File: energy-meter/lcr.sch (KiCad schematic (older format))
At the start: 46 parts, among them Q10 AP3400, Q11 AP3400, Q12 AP3400, Q14 AP3400, U10 SLG47004, U11 SLG47004, U12 SLG47004, U13 XC6227C381MR-G

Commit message: continue changing schematic
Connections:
- wire segments 177 -> 183
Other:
- note added: "6V AC -> 8.5V p-p\n"
- note added: "FIXME:\n- connect input of OpAmps to analog switch to calibrate offset?\n (probably not required for AC)\n- don't use Kelvin measurement for resistors\n -> frees up some analog switches\n- get rid of U10, which is hardly used anymore\n- OUT1=CURR0\n- OUT0B=CURR1\n- VDDA can be 3.3V, I think\n- bias one side of OpAmp to VCC/2"
- note removed: "FIXME:\n- connect input of OpAmps to analog switch to calibrate offset?\n (probably not required for AC)\n- don't use Kelvin measurement for resistors\n -> frees up some analog switches\n- get rid of U10, which is hardly used anymore\n- OUT1=CURR0\n- OUT0B=CURR1\n- VDDA can be 3.3V, I think"
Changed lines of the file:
@@
 CURR1
 Text Notes 12250 4400 0    50   ~ 0
-FIXME:\n- connect input of OpAmps to analog switch to calibrate offset?\n  (probably not required for AC)\n- don't use Kelvin measurement for resistors\n  -> frees up some analog switches\n- get rid of U10, which is hardly used anymore\n- OUT1=CURR0\n- OUT0B=CURR1\n- VDDA can be 3.3V, I think
+FIXME:\n- connect input of OpAmps to analog switch to calibrate offset?\n  (probably not required for AC)\n- don't use Kelvin measurement for resistors\n  -> frees up some analog switches\n- get rid of U10, which is hardly used anymore\n- OUT1=CURR0\n- OUT0B=CURR1\n- VDDA can be 3.3V, I think\n- bias one side of OpAmp to VCC/2
+Wire Wire Line
+	10800 2750 10800 2650
+Wire Wire Line
+	10800 2650 10650 2650
+Connection ~ 10800 2750
+Wire Wire Line
+	10550 3100 10550 3000
+Wire Wire Line
+	10550 3000 10400 3000
+Connection ~ 10400 3000
+Wire Wire Line
+	9750 3550 9750 3300
+Wire Wire Line
+	9750 3300 9900 3300
+Connection ~ 9900 3300
+Text Notes 11850 5800 0    50   ~ 0
+6V AC -> 8.5V p-p\n
 $EndSCHEMATC

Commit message: remove two of the opamps
We can measure the voltage without an amplifier so let's do it. The other
was used for the LCR outputs, which we don't have here.
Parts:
- removed C65, C67, C70, C72: 100n, Capacitor_SMD:C_0603_1608Metric_Pad1.05x0.95mm_HandSolder, symbol Device:C
- removed C79, C80: 4.7p, Capacitor_SMD:C_0603_1608Metric_Pad1.05x0.95mm_HandSolder, symbol Device:C
- removed C81, C82: 1u, Capacitor_SMD:C_0805_2012Metric_Pad1.15x1.40mm_HandSolder, symbol Device:C
- removed FB1, FB3: 600R, 0.5A, Inductor_SMD:L_0603_1608Metric_Pad1.05x0.95mm_HandSolder, symbol Device:Ferrite_Bead_Small
- removed JP20: SolderJumper_2_Open, Jumper:SolderJumper-2_P1.3mm_Open_RoundedPad1.0x1.5mm, symbol Jumper:SolderJumper_2_Open
- removed Q12, Q14: AP3400, Package_TO_SOT_SMD:SOT-23_Handsoldering, symbol Device:Q_NMOS_GSD
- removed R67, R68, R69: 1k, Resistor_SMD:R_0603_1608Metric_Pad1.05x0.95mm_HandSolder, symbol Device:R
- removed R70, R71: 10k, Resistor_SMD:R_0603_1608Metric_Pad1.05x0.95mm_HandSolder, symbol Device:R
- removed R79, R80: 47k, Resistor_SMD:R_0603_1608Metric_Pad1.05x0.95mm_HandSolder, symbol Device:R
- removed R84: 20R, 100 mW, 0.1%, glowstone:R_0603_1608Metric_Pad1.05x0.95mm_HandSolder_Shunt, symbol Device:R_Shunt
- removed R86: 2M, 0.1%, glowstone:R_1210_3225Metric_Pad1.42x2.65mm_HandSolder_Shunt, symbol Device:R_Shunt
- removed R95: 1R, 0.1% (alternative to 2M), glowstone:R_1210_3225Metric_Pad1.42x2.65mm_HandSolder_Shunt, symbol Device:R_Shunt
- removed U10, U12: SLG47004, glowstone:SLG47004, symbol glowstone:SLG47004
- removed U13: XC6227C381MR-G, Package_TO_SOT_SMD:SOT-23-5_HandSoldering, symbol Regulator_Linear:TLV75509PDBV
- added C84: 270p, 1%, Capacitor_SMD:C_0603_1608Metric_Pad1.05x0.95mm_HandSolder, symbol Device:C
- added L4: 470u, Inductor_SMD:L_1210_3225Metric_Pad1.42x2.65mm_HandSolder, symbol Device:L
- added R90, R91: 1k, 1%, Resistor_SMD:R_0603_1608Metric_Pad1.05x0.95mm_HandSolder, symbol Device:R
- R64: value 20R, 100 mW, 0.1% -> 50k, 0.1%
- R85: value 10k, 0.1% -> 50R, 0.1%; footprint glowstone:R_0603_1608Metric_Pad1.05x0.95mm_HandSolder_Shunt -> Resistor_SMD:R_0603_1608Metric_Pad1.05x0.95mm_HandSolder; symbol Device:R_Shunt -> Device:R
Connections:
- net labels removed: 5V, AS0A_1, AS0A_3, AS1A_1, AS1A_3, DAC0, DAC1, OP2_OUT, OP2_OUT_F, OUT0, OUT01_SHORT, OUT0B, OUT1, TEMP2, VDDA1, VDDA3
- wire segments 183 -> 96
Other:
- note added: "FIXME:\n- connect inputs of OpAmp to MCU so it can short them for calibration\n- use resistor dividers to generate reference voltages for calibration,\n VCC side connected to MCU to turn them off\n\n- normal gain should be 4\n- gain 4000 and 4M would be good to have\n\n- add some LEDs for GD32V\n\n- relay\n\n- add optional DC/DC for 3V3 from T2"
- note added: "https://rf-tools.com/lc-filter/"
- note removed: "6V AC -> 8.5V p-p\n"
- note removed: "FIXME:\n- connect input of OpAmps to analog switch to calibrate offset?\n (probably not required for AC)\n- don't use Kelvin measurement for resistors\n -> frees up some analog switches\n- get rid of U10, which is hardly used anymore\n- OUT1=CURR0\n- OUT0B=CURR1\n- VDDA can be 3.3V, I think\n- bias one side of OpAmp to VCC/2"

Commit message: everything done except current measurement
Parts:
- removed D12: SP3012-06UTG, glowstone:UDFN-14_3.5x1.35mm_P0.5mm, symbol glowstone:SP3012-06UTG
- removed Q10: AP3400, Package_TO_SOT_SMD:SOT-23, symbol Device:Q_NMOS_GSD
- removed R54, R55: 10k, Resistor_SMD:R_0603_1608Metric_Pad1.05x0.95mm_HandSolder, symbol Device:R
- Q11: footprint Package_TO_SOT_SMD:SOT-23 -> Package_TO_SOT_SMD:SOT-23_Handsoldering
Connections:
- net labels removed: IN0, IN1, SCL_5V, SDA_5V, VOLTAGE0, VOLTAGE1
- wire segments 96 -> 61
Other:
- note added: "FIXME:\n- connect inputs of OpAmp to MCU so it can short them for calibration\n- use resistor dividers to generate reference voltages for calibration,\n VCC side connected to MCU to turn them off\n\n- normal gain should be 4\n- gain 4000 and 4M would be good to have\n\n- add some LEDs for GD32V\n\n- relay\n\n- add optional DC/DC for 3V3 from T2\n\n- remove LC filter and replace by one that is bef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"
- note removed: "FIXME:\n- connect inputs of OpAmp to MCU so it can short them for calibration\n- use resistor dividers to generate reference voltages for calibration,\n VCC side connected to MCU to turn them off\n\n- normal gain should be 4\n- gain 4000 and 4M would be good to have\n\n- add some LEDs for GD32V\n\n- relay\n\n- add optional DC/DC for 3V3 from T2"
- moved on the sheet: R52, R53

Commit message: DRC, add header for I2C
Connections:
- net labels removed: VDDA
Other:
- note added: "FIXME:\n- connect inputs of OpAmp to MCU so it can short them for calibration\n- use resistor dividers to generate reference voltages for calibration,\n VCC side connected to MCU to turn them off\n\n- normal gain should be 4\n- gain 4000 and 4M would be good to have\n\n- remove LC filter and replace by one that is before the opamp?"
- note removed: "FIXME:\n- connect inputs of OpAmp to MCU so it can short them for calibration\n- use resistor dividers to generate reference voltages for calibration,\n VCC side connected to MCU to turn them off\n\n- normal gain should be 4\n- gain 4000 and 4M would be good to have\n\n- add some LEDs for GD32V\n\n- relay\n\n- add optional DC/DC for 3V3 from T2\n\n- remove LC filter and replace by one that is bef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"
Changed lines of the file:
@@
-$EndComp
-$Comp
-L power:VDDA #PWR0119
-U 1 1 605C4057
-P 3900 5650
-F 0 "#PWR0119" H 3900 5500 50  0001 C CNN
-F 1 "VDDA" H 3917 5823 50  0000 C CNN
-F 2 "" H 3900 5650 50  0001 C CNN
-F 3 "" H 3900 5650 50  0001 C CNN
-	1    3900 5650
-	1    0    0    -1
 $EndComp
 $Comp
@@
 CURR1
 Text Notes 12250 4400 0    50   ~ 0
-FIXME:\n- connect inputs of OpAmp to MCU so it can short them for calibration\n- use resistor dividers to generate reference voltages for calibration,\n  VCC side connected to MCU to turn them off\n\n- normal gain should be 4\n- gain 4000 and 4M would be good to have\n\n- add some LEDs for GD32V\n\n- relay\n\n- add optional DC/DC for 3V3 from T2\n\n- remove LC filter and replace by one that is before the opamp?
+FIXME:\n- connect inputs of OpAmp to MCU so it can short them for calibration\n- use resistor dividers to generate reference voltages for calibration,\n  VCC side connected to MCU to turn them off\n\n- normal gain should be 4\n- gain 4000 and 4M would be good to have\n\n- remove LC filter and replace by one that is before the opamp?
 Text Label 4600 4850 2    50   ~ 0
 CURR1
@@
 	0    1    1    0
 $EndComp
+$Comp
+L power:+3V3 #PWR0119
+U 1 1 60CCAFAF
+P 3900 5650
+F 0 "#PWR0119" H 3900 5500 50  0001 C CNN
+F 1 "+3V3" H 3915 5823 50  0000 C CNN
+F 2 "" H 3900 5650 50  0001 C CNN
+F 3 "" H 3900 5650 50  0001 C CNN
+	1    3900 5650
+	1    0    0    -1
+$EndComp
 $EndSCHEMATC

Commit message: 2nd relay needs an additional driver if we want to use both of them
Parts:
- removed Q11: AP3400, Package_TO_SOT_SMD:SOT-23_Handsoldering, symbol Device:Q_NMOS_GSD
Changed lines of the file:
@@
 Wire Wire Line
 	10100 2600 10100 3350
-$Comp
-L Device:Q_NMOS_GSD Q?
-U 1 1 6091EE3A
-P 12650 2100
-AR Path="/60846F2E/6091EE3A" Ref="Q?"  Part="1"
-AR Path="/60514CC5/6091EE3A" Ref="Q11"  Part="1"
-AR Path="/607B74C2/6091EE3A" Ref="Q11"  Part="1"
-F 0 "Q11" H 12856 2146 50  0000 L CNN
-F 1 "AP3400" H 12856 2055 50  0000 L CNN
-F 2 "Package_TO_SOT_SMD:SOT-23_Handsoldering" H 12850 2200 50  0001 C CNN
-F 3 "https://datasheet.lcsc.com/szlcsc/1901071504_ShenZhen-Quan-Li-Semiconductor-AP3400_C353070.pdf" H 12650 2100 50  0001 C CNN
-F 4 "AP3400, C353070, HSS2306A, C518790, AO3400A, C700953" H 12650 2100 50  0001 C CNN "LCSC"
-	1    12650 2100
-	0    1    1    0
-$EndComp
 Text HLabel 2500 4850 0    50   Input ~ 0
 SDA

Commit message: adjust voltage divider to somewhat work if transformer is also used for VCC
In that case, we will only see one half of the wave.
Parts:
- added U2: MCP6V96T-E/OT, Package_TO_SOT_SMD:SOT-23-5, symbol Amplifier_Operational:MCP6L91T-EOT
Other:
- note added: "FIXME:\n- use OP07 as suggested here?\n https://datasheet.lcsc.com/szlcsc/1810010312_Qingxian-Zeming-Langxi-Elec-ZMCT104C_C84212.pdf\n -> first stage with MCP and similar to that ^^ (see my LTSpice simulation),\n second and third stage with 1000x gain, connect all intermediate signals to\n ADC so GD32 can choose gain by choosing the right signal\n- connect inputs of OpAmp to MCU so it can short t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"
- note removed: "FIXME:\n- connect inputs of OpAmp to MCU so it can short them for calibration\n- use resistor dividers to generate reference voltages for calibration,\n VCC side connected to MCU to turn them off\n\n- normal gain should be 4\n- gain 4000 and 4M would be good to have\n\n- remove LC filter and replace by one that is before the opamp?"
- note removed: "For 3.3V/2+-0.5V:\n49.45k and 65.55k"
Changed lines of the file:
@@
 Text Label 7500 2950 1    50   ~ 0
 VDDA2
-Text Notes 7600 4050 0    50   ~ 0
-For 3.3V/2+-0.5V:\n49.45k and 65.55k
 $Comp
 L Device:R R85
@@
 Text Label 8600 3350 0    50   ~ 0
 CURR1
-Text Notes 12250 4400 0    50   ~ 0
-FIXME:\n- connect inputs of OpAmp to MCU so it can short them for calibration\n- use resistor dividers to generate reference voltages for calibration,\n  VCC side connected to MCU to turn them off\n\n- normal gain should be 4\n- gain 4000 and 4M would be good to have\n\n- remove LC filter and replace by one that is before the opamp?
+Text Notes 7450 6100 0    50   ~ 0
+FIXME:\n- use OP07 as suggested here?\n  https://datasheet.lcsc.com/szlcsc/1810010312_Qingxian-Zeming-Langxi-Elec-ZMCT104C_C84212.pdf\n  -> first stage with MCP and similar to that ^^ (see my LTSpice simulation),\n  second and third stage with 1000x gain, connect all intermediate signals to\n  ADC so GD32 can choose gain by choosing the right signal\n- connect inputs of OpAmp to MCU so it can short them for calibration\n- use resistor dividers to generate reference voltages for calibration,\n  VCC side connected to MCU to turn them off\n\n- normal gain should be 4\n- gain 4000 and 4M would be good to have\n\n- remove LC filter and replace by one that is before the opamp?
 Text Label 4600 4850 2    50   ~ 0
 CURR1
@@
 	1    0    0    -1
 $EndComp
+$Comp
+L Amplifier_Operational:MCP6L91T-EOT U2
+U 1 1 60E518DB
+P 8750 2000
+F 0 "U2" H 9094 2046 50  0000 L CNN
+F 1 "MCP6V96T-E/OT" H 9094 1955 50  0000 L CNN
+F 2 "Package_TO_SOT_SMD:SOT-23-5" H 8650 1800 50  0001 L CNN
+F 3 "https://www.mouser.de/datasheet/2/268/MCP6V96_Family_Data_Sheet_DS20006467A-1948680.pdf" H 8750 2200 50  0001 C CNN
+	1    8750 2000
+	1    0    0    -1
+$EndComp

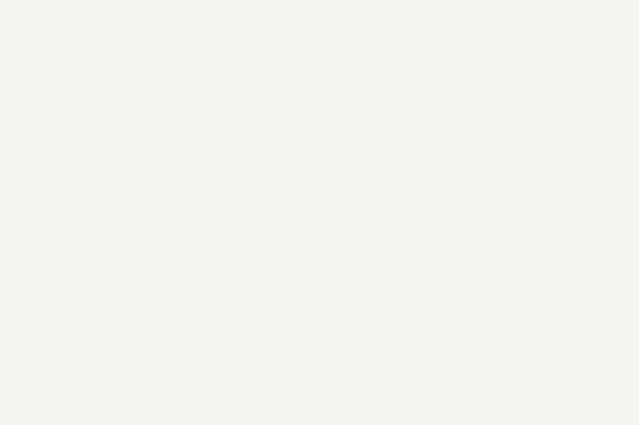
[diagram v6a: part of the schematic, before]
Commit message: use solid state relays for calibration
That way, we have enough space for two of them. The alternative relay
shares space with the other relay because only one of them will be used.
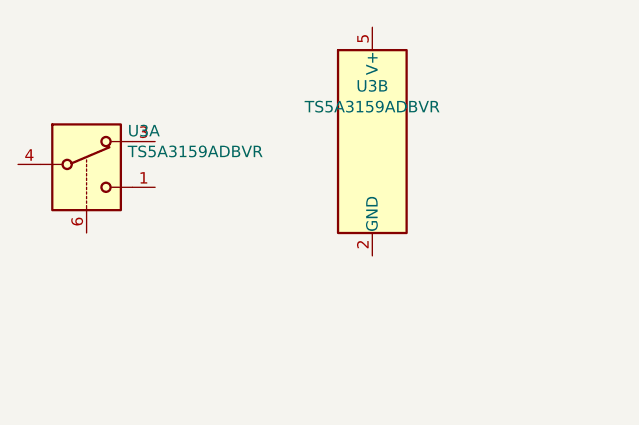
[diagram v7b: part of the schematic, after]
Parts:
- added U3: TS5A3159ADBVR, Package_TO_SOT_SMD:SOT-23-6, symbol Analog_Switch:TS5A3159ADBVR
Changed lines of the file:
@@
 $Descr A4 11693 8268
 encoding utf-8
-Sheet 2 2
+Sheet 2 3
 Title ""
 Date ""
@@
 	1    0    0    -1
 $EndComp
+$Comp
+L Analog_Switch:TS5A3159ADBVR U3
+U 2 1 60F119FA
+P 2400 1350
+F 0 "U3" H 2400 1592 50  0000 C CNN
+F 1 "TS5A3159ADBVR" H 2400 1501 50  0000 C CNN
+F 2 "Package_TO_SOT_SMD:SOT-23-6" H 2400 1050 50  0001 C CNN
+F 3 "http://www.ti.com/lit/ds/symlink/ts5a3159a.pdf" H 2400 1350 50  0001 C CNN
+	2    2400 1350
+	1    0    0    -1
+$EndComp
+$Comp
+L Analog_Switch:TS5A3159ADBVR U3
+U 1 1 60F12E08
+P 1150 1350
+F 0 "U3" H 1330 1396 50  0000 L CNN
+F 1 "TS5A3159ADBVR" H 1330 1305 50  0000 L CNN
+F 2 "Package_TO_SOT_SMD:SOT-23-6" H 1150 1050 50  0001 C CNN
+F 3 "http://www.ti.com/lit/ds/symlink/ts5a3159a.pdf" H 1150 1350 50  0001 C CNN
+	1    1150 1350
+	1    0    0    -1
+$EndComp

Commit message: add opamps
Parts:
- removed C66, C68: 100n, Capacitor_SMD:C_0603_1608Metric_Pad1.05x0.95mm_HandSolder, symbol Device:C
- removed C77, C78: 4.7p, Capacitor_SMD:C_0603_1608Metric_Pad1.05x0.95mm_HandSolder, symbol Device:C
- removed C84: 270p, 1%, Capacitor_SMD:C_0603_1608Metric_Pad1.05x0.95mm_HandSolder, symbol Device:C
- removed FB2: 600R, 0.5A, Inductor_SMD:L_0603_1608Metric_Pad1.05x0.95mm_HandSolder, symbol Device:Ferrite_Bead_Small
- removed L4: 470u, Inductor_SMD:L_1210_3225Metric_Pad1.42x2.65mm_HandSolder, symbol Device:L
- removed R52, R53, R72, R73: 10k, Resistor_SMD:R_0603_1608Metric_Pad1.05x0.95mm_HandSolder, symbol Device:R
- removed R64: 50k, 0.1%, Resistor_SMD:R_0603_1608Metric_Pad1.05x0.95mm_HandSolder, symbol Device:R
- removed R66: 1k, Resistor_SMD:R_0603_1608Metric_Pad1.05x0.95mm_HandSolder, symbol Device:R
- removed R74, R75: 47k, Resistor_SMD:R_0603_1608Metric_Pad1.05x0.95mm_HandSolder, symbol Device:R
- removed R85: 50R, 0.1%, Resistor_SMD:R_0603_1608Metric_Pad1.05x0.95mm_HandSolder, symbol Device:R
- removed R90, R91: 1k, 1%, Resistor_SMD:R_0603_1608Metric_Pad1.05x0.95mm_HandSolder, symbol Device:R
- removed U11: SLG47004, glowstone:SLG47004, symbol glowstone:SLG47004
- added C10, C13: 10n, Capacitor_SMD:C_0603_1608Metric_Pad1.05x0.95mm_HandSolder, symbol Device:C
- added C11, C7: 10u, Capacitor_SMD:C_0805_2012Metric_Pad1.15x1.40mm_HandSolder, symbol Device:C
- added C12, C14, C15, C16, C17, C8, C9: 100n, Capacitor_SMD:C_0603_1608Metric_Pad1.05x0.95mm_HandSolder, symbol Device:C
- added C18, C19: 270p, 1%, Capacitor_SMD:C_0603_1608Metric_Pad1.05x0.95mm_HandSolder, symbol Device:C
- added D6, D8, D9: ESD5Z5.0T1G, Diode_SMD:D_SOD-523, symbol Device:D_Zener
- added FB1: 600R, 0.5A, Inductor_SMD:L_0603_1608Metric_Pad1.05x0.95mm_HandSolder, symbol Device:Ferrite_Bead_Small
- added JP11, JP12: SolderJumper_2_Open, Jumper:SolderJumper-2_P1.3mm_Open_RoundedPad1.0x1.5mm, symbol Jumper:SolderJumper_2_Open
- added NT1: Net-Tie_2, NetTie:NetTie-2_SMD_Pad2.0mm, symbol Device:Net-Tie_2
- added R13, R16: 0R, Resistor_SMD:R_0603_1608Metric_Pad1.05x0.95mm_HandSolder, symbol Device:R
- added R14, R15, R25: 10k, 1%, Resistor_SMD:R_0603_1608Metric_Pad1.05x0.95mm_HandSolder, symbol Device:R
- added R17: 100k, Resistor_SMD:R_0603_1608Metric_Pad1.05x0.95mm_HandSolder, symbol Device:R
- added R18, R19: 10R, Resistor_SMD:R_0603_1608Metric_Pad1.05x0.95mm_HandSolder, symbol Device:R
- added R20: 220R, 1%, Resistor_SMD:R_0603_1608Metric_Pad1.05x0.95mm_HandSolder, symbol Device:R
- added R21: 220k, 1%, Resistor_SMD:R_0603_1608Metric_Pad1.05x0.95mm_HandSolder, symbol Device:R
- added R22, R23, R24, R27: 1k, 1%, Resistor_SMD:R_0603_1608Metric_Pad1.05x0.95mm_HandSolder, symbol Device:R
- added R26: 100k, 1%, Resistor_SMD:R_0603_1608Metric_Pad1.05x0.95mm_HandSolder, symbol Device:R
- added U10, U12: MCP6V96T-E/OT, Package_TO_SOT_SMD:SOT-23-5, symbol Amplifier_Operational:MCP6L91T-EOT
- added U11, U8: TS5A3159ADBVR, Package_TO_SOT_SMD:SOT-23-6, symbol Analog_Switch:TS5A3159ADBVR
- added U7: LP2951-3.3_SOIC, Package_SO:SOIC-8_3.9x4.9mm_P1.27mm, symbol Regulator_Linear:LP2951-3.3_SOIC
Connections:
- net labels added: +5V, BIAS, BIAS_MCU, CURRENT_OUT0, CURRENT_OUT1, ENA_1000x, ENA_100x, GNDA, SHORT_CURRENT, TUNE_OFFSET0, VDDA
- net labels removed: +3V3, AS0A_2, AS1A_2, CURR0, CURR1, OP1_OUT, OP1_OUT_F, SCL, SDA, TEMP1, VDDA2
- wire segments 61 -> 97
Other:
- note removed: "FIXME:\n- use OP07 as suggested here?\n https://datasheet.lcsc.com/szlcsc/1810010312_Qingxian-Zeming-Langxi-Elec-ZMCT104C_C84212.pdf\n -> first stage with MCP and similar to that ^^ (see my LTSpice simulation),\n second and third stage with 1000x gain, connect all intermediate signals to\n ADC so GD32 can choose gain by choosing the right signal\n- connect inputs of OpAmp to MCU so it can short t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"
- note removed: "https://rf-tools.com/lc-filter/"
- note removed: "open, for I2C address"
- moved on the sheet: U2, U3A, U3B
